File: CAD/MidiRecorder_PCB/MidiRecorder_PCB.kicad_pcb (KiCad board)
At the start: 2 copper layers, 66 x 50.8 mm, 15 parts, among them J1 5V DC, J2 MIDI IN, J3 MIDI THRU, J4 RGB OUT, U1 HT7333, U2 6N138, U3 LogicLevelConverter, U4 ESP32 WROOM

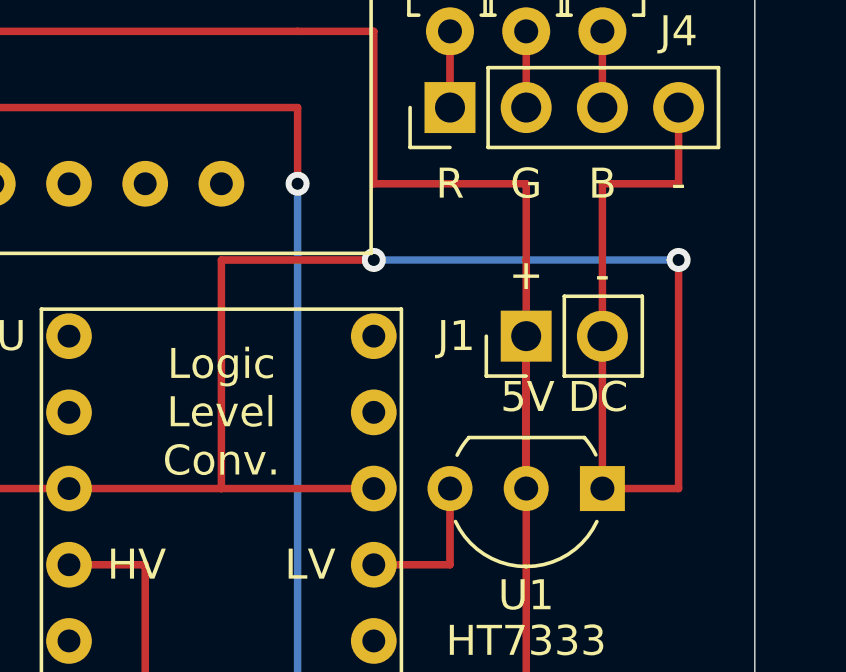
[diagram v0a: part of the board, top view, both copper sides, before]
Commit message: fix: Disconnect 5V from 3V3 oops
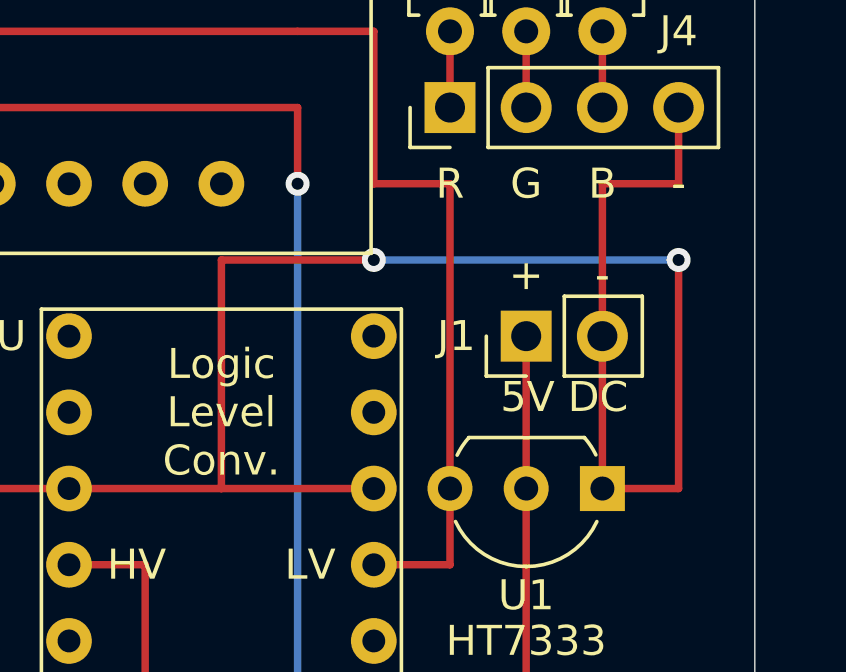
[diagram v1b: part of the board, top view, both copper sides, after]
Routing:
- net +3V3: track 71.1 -> 68.6 mm
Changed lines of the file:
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@@
     (thickness 1.6)
     (drawings 32)
-    (tracks 83)
+    (tracks 82)
     (zones 0)
     (modules 15)
@@
   (segment (start 124.46 88.9) (end 86.36 88.9) (width 0.25) (layer F.Cu) (net 19))
   (segment (start 86.36 88.9) (end 86.36 93.98) (width 0.25) (layer F.Cu) (net 19))
-  (segment (start 132.08 104.14) (end 132.08 96.52) (width 0.25) (layer F.Cu) (net 19))
   (segment (start 129.54 104.14) (end 129.54 106.68) (width 0.25) (layer F.Cu) (net 19))
   (segment (start 129.54 106.68) (end 127 106.68) (width 0.25) (layer F.Cu) (net 19))
-  (segment (start 132.08 96.52) (end 132.08 93.98) (width 0.25) (layer F.Cu) (net 19))
   (segment (start 124.46 88.9) (end 127 88.9) (width 0.25) (layer F.Cu) (net 19))
   (segment (start 127 88.9) (end 127 93.98) (width 0.25) (layer F.Cu) (net 19))
-  (segment (start 127 93.98) (end 132.08 93.98) (width 0.25) (layer F.Cu) (net 19))
+  (segment (start 129.54 104.14) (end 129.54 93.98) (width 0.25) (layer F.Cu) (net 19))
+  (segment (start 129.54 93.98) (end 127 93.98) (width 0.25) (layer F.Cu) (net 19))
   (segment (start 99.06 93.98) (end 99.06 91.44) (width 0.25) (layer F.Cu) (net 29))
   (segment (start 99.06 91.44) (end 124.46 91.44) (width 0.25) (layer F.Cu) (net 29))
